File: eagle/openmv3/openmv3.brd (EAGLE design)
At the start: 35.6 x 44.5 mm, 63 parts, among them J3 CON_HEADER_1X03, J4 CON_HEADER_1X03, Q1 MOSFET, U12 STM32F407LQFP100, U2 USD-47571, U4 TPS768, U8 VREG_28, U9 OV2640, X2 USB-MICROB

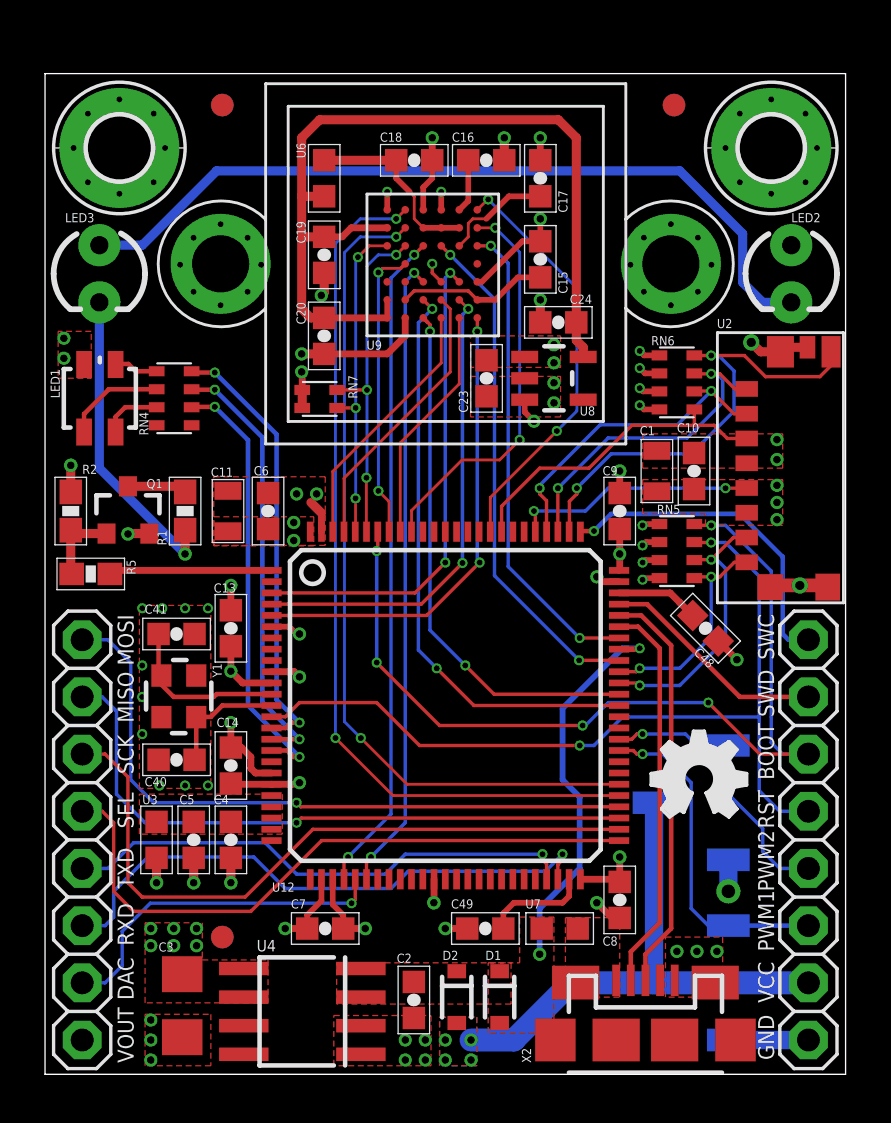
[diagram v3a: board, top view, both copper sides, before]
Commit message: Update design files
* Replace 1A TI regulator with BD 500mA.
* Replace ORing diodes with one dual common cathode.
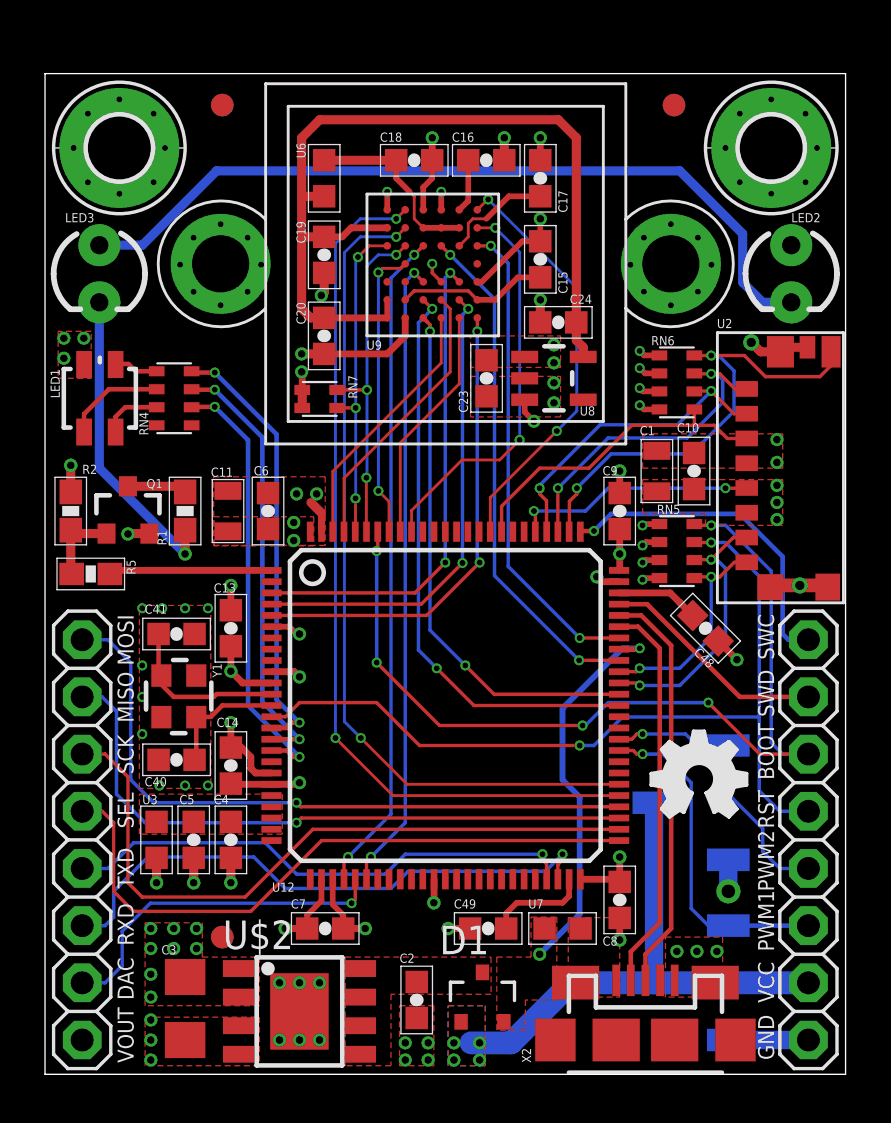
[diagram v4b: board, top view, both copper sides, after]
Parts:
- removed D2: (no value), sfe:SOD-323
- removed U4: TPS768, mux:SOIC8
- added U$2: BD33IA, mux:HTSOP-J8
- D1: value (none) -> BAT54C; device sfe:SOD-323 -> diode:SOT23
- moved D1 0.76 mm to (19.4, 3.43), turned to 0 degrees
- moved U$3 0.25 mm to (17.8, 1.52)
- moved C3 0.18 mm to (6.22, 2.92)
- moved C2 0.13 mm to (16.5, 3.30)
- moved C49 0.13 mm to (19.7, 6.48)
- moved U7 0.13 mm to (23.0, 6.48)
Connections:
- net GND: now also U$2.3, U$2.P$1; no longer U4.1, U4.2
- net RAW: now also D1.1; no longer D2.2
- net VCC: now also U$2.1, U$2.2; no longer U4.5, U4.6
- net VIN: now also D1.3, U$2.5, U$2.8; no longer D1.1, D2.1, U4.3, U4.4
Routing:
- net GND: track 52.8 -> 53.8 mm, vias 55 -> 61
- net VCC: vias 30 -> 33

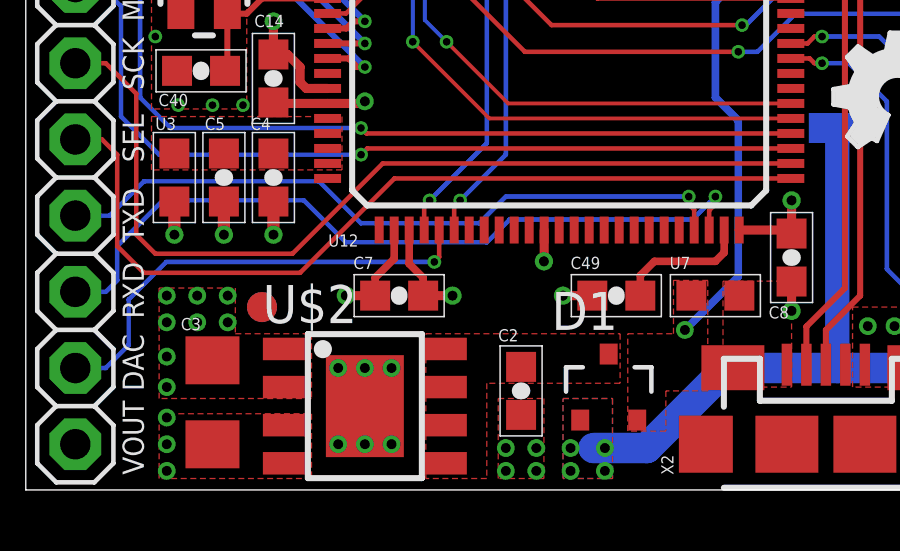
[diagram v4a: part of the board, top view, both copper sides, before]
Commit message: Update silk screen
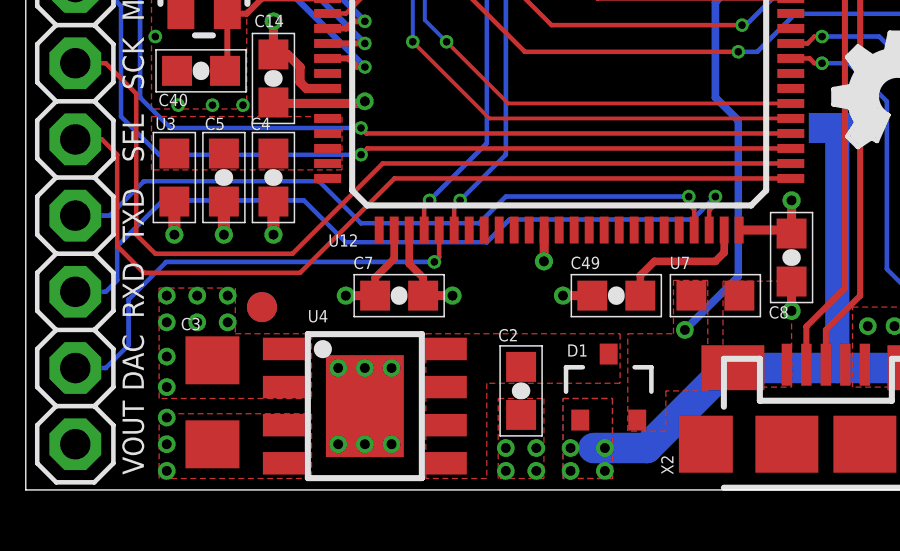
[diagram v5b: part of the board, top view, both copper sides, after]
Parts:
- U12: value STM32F407LQFP100 -> STM32F427-LQFP100
- renumbered U$1 to U1, U$2 to U4
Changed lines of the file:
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@@
 <layer number="23" name="tOrigins" color="15" fill="1" visible="yes" active="yes"/>
 <layer number="24" name="bOrigins" color="15" fill="1" visible="yes" active="yes"/>
-<layer number="25" name="tNames" color="7" fill="1" visible="no" active="yes"/>
-<layer number="26" name="bNames" color="7" fill="1" visible="no" active="yes"/>
+<layer number="25" name="tNames" color="7" fill="1" visible="yes" active="yes"/>
+<layer number="26" name="bNames" color="7" fill="1" visible="yes" active="yes"/>
 <layer number="27" name="tValues" color="7" fill="1" visible="no" active="yes"/>
 <layer number="28" name="bValues" color="7" fill="1" visible="no" active="yes"/>
-<layer number="29" name="tStop" color="7" fill="3" visible="yes" active="yes"/>
-<layer number="30" name="bStop" color="7" fill="6" visible="yes" active="yes"/>
+<layer number="29" name="tStop" color="7" fill="3" visible="no" active="yes"/>
+<layer number="30" name="bStop" color="7" fill="6" visible="no" active="yes"/>
 <layer number="31" name="tCream" color="7" fill="4" visible="no" active="yes"/>
 <layer number="32" name="bCream" color="7" fill="5" visible="no" active="yes"/>
@@
 <attribute name="VALUE" x="36.576" y="32.893" size="1.27" layer="27" rot="R270"/>
 </element>
-<element name="U$1" library="omnivision" package="LENSMOUNT-20MM" value="LENSMOUNT20MM" x="17.8" y="36" smashed="yes"/>
+<element name="U1" library="omnivision" package="LENSMOUNT-20MM" value="LENSMOUNT20MM" x="17.8" y="36" smashed="yes"/>
 <element name="H2" library="holes" package="2,8-PAD" value="MOUNT-PAD-ROUND2.8" x="3.302" y="41.148" smashed="yes" rot="R90"/>
 <element name="RN6" library="resistor-dil" package="EXBV8V" value="10K" x="28.067" y="30.734" smashed="yes" rot="R270">
@@
 </element>
 <element name="LOGO1" library="iofault" package="OSHW_FILLX150_NOTEXT" value="OSHW_LOGO_FILLX0150-NT" x="26.924" y="11.43" smashed="yes"/>
-<element name="U12" library="mux" package="LQFP100" value="STM32F407LQFP100" x="17.78" y="16.383" smashed="yes">
+<element name="U12" library="mux" package="LQFP100" value="STM32F427-LQFP100" x="17.78" y="16.383" smashed="yes">
 <attribute name="NAME" x="10.081" y="8.112" size="0.4064" layer="25" font="vector" ratio="20"/>
 <attribute name="VALUE" x="12.645" y="15.288" size="1.27" layer="27"/>
@@
 </element>
 <element name="U$3" library="openmv" package="OMV-LOGO" value="" x="17.78" y="1.524" rot="MR0"/>
-<element name="U$2" library="mux" package="HTSOP-J8" value="BD33IA" x="11.303" y="2.794" rot="R270"/>
-<element name="D1" library="diode" package="SOT23" value="BAT54C" x="19.431" y="3.429"/>
+<element name="U4" library="mux" package="HTSOP-J8" value="BD33IA" x="11.303" y="2.794" smashed="yes" rot="R270">
+<attribute name="NAME" x="9.398" y="5.588" size="0.4064" layer="25" font="vector" ratio="20"/>
+<attribute name="VALUE" x="7.998" y="-1.043" size="1.27" layer="27"/>
+</element>
+<element name="D1" library="diode" package="SOT23" value="BAT54C" x="19.431" y="3.429" smashed="yes">
+<attribute name="NAME" x="18.034" y="4.445" size="0.4064" layer="25" font="vector" ratio="20"/>
+<attribute name="VALUE" x="17.526" y="0.254" size="1.27" layer="27"/>
+</element>
 </elements>
 <signals>
@@
 <vertex x="13.335" y="5.207"/>
 </polygon>
-<contactref element="U$2" pad="5"/>
-<contactref element="U$2" pad="8"/>
+<contactref element="U4" pad="5"/>
+<contactref element="U4" pad="8"/>
 <contactref element="D1" pad="3"/>
 </signal>
@@
 <wire x1="17.28" y1="7.628" x2="17.272" y2="7.62" width="0.3048" layer="1"/>
 <via x="32.512" y="26.162" extent="1-16" drill="0.3302"/>
-<contactref element="U$2" pad="3"/>
-<contactref element="U$2" pad="P$1"/>
+<contactref element="U4" pad="3"/>
+<contactref element="U4" pad="P$1"/>
 <via x="12.192" y="4.064" extent="1-16" drill="0.3302"/>
 <via x="12.192" y="1.524" extent="1-16" drill="0.3302"/>
@@
 <wire x1="25.411" y1="8.663" x2="25.527" y2="8.547" width="0.3048" layer="1"/>
 <wire x1="25.527" y1="8.547" x2="25.527" y2="9.652" width="0.3048" layer="1"/>
-<contactref element="U$2" pad="1"/>
-<contactref element="U$2" pad="2"/>
+<contactref element="U4" pad="1"/>
+<contactref element="U4" pad="2"/>
 <via x="4.699" y="3.429" extent="1-16" drill="0.3302"/>
 <via x="4.699" y="4.445" extent="1-16" drill="0.3302"/>
@@
 </signal>
 </signals>
+<errors>
+</errors>
 </board>
 </drawing>
